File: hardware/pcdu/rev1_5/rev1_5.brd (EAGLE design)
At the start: 90 x 16.2 mm, 11 parts, among them IC1 74HC595N, X1 MUSBV, X2 MUSBV, X3 MUSBV, X4 MUSBV, X7 22-23-2041, X8 22-23-2041

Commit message: Added PCU board, updated revision 5 PDU board
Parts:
- removed X6: (no value), con-wago-500:W237-102
- moved X5 0.91 mm to (24.1, 12.3)
- moved U$1 0.91 mm to (22.6, 5.94)
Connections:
- net GND: no longer X6.2
- net VCC: no longer X6.1
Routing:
- net GND: track 8.89 -> 0.00 mm
- net N$2: track 39.3 -> 45.1 mm
- net SIN: track 50.2 -> 47.8 mm
- net N$1: track 44.9 -> 46.0 mm
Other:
- board text added: "5VPDU Rev1.5"
- board text added: "GND"
- board text added: "IN"
- board text added: "OUT"
- board text added: "RCK"
- board text added: "SCK"
- board text added: "SER"
- board text added: "VCC"
- board text added: "by Denis Lavrov"
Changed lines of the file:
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@@
 <setting verticaltext="up"/>
 </settings>
-<grid distance="12" unitdist="mil" unit="mil" style="lines" multiple="1" display="no" altdistance="0.025" altunitdist="inch" altunit="inch"/>
+<grid distance="12" unitdist="mil" unit="mil" style="lines" multiple="1" display="no" altdistance="6" altunitdist="mil" altunit="mil"/>
 <layers>
 <layer number="1" name="Top" color="4" fill="1" visible="yes" active="yes"/>
@@
 <wire x1="90" y1="16.18" x2="0" y2="16.18" width="0" layer="20"/>
 <wire x1="0" y1="16.18" x2="0" y2="0" width="0" layer="20"/>
+<text x="73.152" y="13.4112" size="1.778" layer="21">5VPDU Rev1.5</text>
+<text x="71.628" y="0.6096" size="1.778" layer="21">by Denis Lavrov</text>
+<text x="11.2776" y="0.9144" size="1.778" layer="21">IN</text>
+<text x="11.2776" y="14.0208" size="1.778" layer="21">OUT</text>
+<text x="2.7432" y="8.5344" size="0.6096" layer="21" rot="R180">GND</text>
+<text x="5.1816" y="8.5344" size="0.6096" layer="21" rot="R180">RCK</text>
+<text x="7.62" y="8.5344" size="0.6096" layer="21" rot="R180">SCK</text>
+<text x="10.0584" y="8.5344" size="0.6096" layer="21" rot="R180">SER</text>
+<text x="20.1168" y="5.4864" size="1.016" layer="21">VCC</text>
+<text x="25.273" y="5.4864" size="1.016" layer="21">GND</text>
 </plain>
 <attributes>
@@
 <elements>
 <element name="IC1" library="74xx-eu" package="DIL16" value="74HC595N" x="49.53" y="7.47" rot="R180"/>
-<element name="U$1" library="FDC6305N" package="FDC6305" value="FDC6305N" x="22.5552" y="6.858" rot="MR90"/>
+<element name="U$1" library="FDC6305N" package="FDC6305" value="FDC6305N" x="22.5552" y="5.9436" rot="MR90"/>
 <element name="U$2" library="FDC6305N" package="FDC6305" value="FDC6305N" x="73.7616" y="9.652" rot="MR90"/>
-<element name="X5" library="con-wago-500" package="W237-102" value="" x="24.13" y="13.2588">
-<attribute name="OC_NEWARK" value="70K9898" x="24.13" y="13.2588" size="1.778" layer="27" display="off"/>
-<attribute name="MF" value="" x="24.13" y="13.2588" size="1.778" layer="27" display="off"/>
-<attribute name="OC_FARNELL" value="unknown" x="24.13" y="13.2588" size="1.778" layer="27" display="off"/>
-<attribute name="MPN" value="237-102" x="24.13" y="13.2588" size="1.778" layer="27" display="off"/>
+<element name="X5" library="con-wago-500" package="W237-102" value="" x="24.13" y="12.3444">
+<attribute name="OC_NEWARK" value="70K9898" x="24.13" y="12.3444" size="1.778" layer="27" display="off"/>
+<attribute name="MF" value="" x="24.13" y="12.3444" size="1.778" layer="27" display="off"/>
+<attribute name="OC_FARNELL" value="unknown" x="24.13" y="12.3444" size="1.778" layer="27" display="off"/>
+<attribute name="MPN" value="237-102" x="24.13" y="12.3444" size="1.778" layer="27" display="off"/>
 </element>
-<element name="X6" library="con-wago-500" package="W237-102" value="" x="24.13" y="1.8796" rot="R180">
-<attribute name="OC_NEWARK" value="70K9898" x="24.13" y="1.8796" size="1.778" layer="27" rot="R180" display="off"/>
-<attribute name="MF" value="" x="24.13" y="1.8796" size="1.778" layer="27" rot="R180" display="off"/>
-<attribute name="OC_FARNELL" value="unknown" x="24.13" y="1.8796" size="1.778" layer="27" rot="R180" display="off"/>
-<attribute name="MPN" value="237-102" x="24.13" y="1.8796" size="1.778" layer="27" rot="R180" display="off"/>
-</element>
-<element name="X7" library="con-molex" package="22-23-2041" value="22-23-2041" x="5.73" y="3.81" rot="R180">
+<element name="X7" library="con-molex" package="22-23-2041" value="22-23-2041" x="5.73" y="3.81" smashed="yes" rot="R180">
 <attribute name="OC_NEWARK" value="38C0355" x="5.73" y="3.81" size="1.778" layer="27" rot="R180" display="off"/>
 <attribute name="MF" value="MOLEX" x="5.73" y="3.81" size="1.778" layer="27" rot="R180" display="off"/>
@@
 <attribute name="MPN" value="22-23-2041" x="5.73" y="3.81" size="1.778" layer="27" rot="R180" display="off"/>
 </element>
-<element name="X8" library="con-molex" package="22-23-2041" value="22-23-2041" x="5.73" y="12.7" rot="R180">
+<element name="X8" library="con-molex" package="22-23-2041" value="22-23-2041" x="5.73" y="12.7" smashed="yes" rot="R180">
 <attribute name="OC_NEWARK" value="38C0355" x="5.73" y="12.7" size="1.778" layer="27" rot="R180" display="off"/>
 <attribute name="MF" value="MOLEX" x="5.73" y="12.7" size="1.778" layer="27" rot="R180" display="off"/>
@@
 <signal name="VCC">
 <contactref element="X5" pad="1"/>
-<contactref element="X6" pad="1"/>
 <contactref element="IC1" pad="16"/>
 <contactref element="IC1" pad="10"/>
@@
 <contactref element="U$2" pad="S2"/>
 <contactref element="X5" pad="2"/>
-<contactref element="X6" pad="2"/>
 <contactref element="X7" pad="4"/>
 <contactref element="X8" pad="4"/>
@@
 <contactref element="U$1" pad="S1"/>
 <contactref element="U$2" pad="S1"/>
-<wire x1="1.92" y1="12.7" x2="1.92" y2="3.81" width="0.1524" layer="1"/>
 <polygon width="0.1524" layer="16">
 <vertex x="0" y="16.1544"/>
@@
 <contactref element="IC1" pad="15"/>
 <contactref element="U$1" pad="G1"/>
-<wire x1="55.88" y1="3.66" x2="55.88" y2="5.7912" width="0.1524" layer="16"/>
-<wire x1="55.88" y1="5.7912" x2="37.1856" y2="5.7912" width="0.1524" layer="16"/>
-<wire x1="37.1856" y1="5.7912" x2="37.1856" y2="11.2776" width="0.1524" layer="16"/>
-<wire x1="37.1856" y1="11.2776" x2="32.9184" y2="11.2776" width="0.1524" layer="16"/>
-<wire x1="32.9184" y1="11.2776" x2="32.9184" y2="7.9248" width="0.1524" layer="16"/>
-<wire x1="32.9184" y1="7.9248" x2="23.1648" y2="7.9248" width="0.1524" layer="16"/>
-<wire x1="23.1648" y1="7.9248" x2="23.1648" y2="9.058" width="0.1524" layer="16"/>
-<wire x1="23.1648" y1="9.058" x2="23.1052" y2="9.058" width="0.1524" layer="16"/>
+<wire x1="55.88" y1="3.66" x2="55.88" y2="7.0104" width="0.1524" layer="16"/>
+<wire x1="55.88" y1="7.0104" x2="37.4904" y2="7.0104" width="0.1524" layer="16"/>
+<wire x1="37.4904" y1="7.0104" x2="37.4904" y2="11.2776" width="0.1524" layer="16"/>
+<wire x1="37.4904" y1="11.2776" x2="32.3088" y2="11.2776" width="0.1524" layer="16"/>
+<wire x1="32.3088" y1="11.2776" x2="32.3088" y2="6.858" width="0.1524" layer="16"/>
+<wire x1="32.3088" y1="6.858" x2="23.1648" y2="6.858" width="0.1524" layer="16"/>
+<wire x1="23.1648" y1="6.858" x2="23.1648" y2="7.8388" width="0.1524" layer="16"/>
+<wire x1="23.1648" y1="7.8388" x2="23.1052" y2="8.1436" width="0.1524" layer="16"/>
 </signal>
 <signal name="N$2">
 <contactref element="IC1" pad="1"/>
 <contactref element="U$1" pad="G2"/>
-<wire x1="58.42" y1="11.28" x2="58.42" y2="9.7536" width="0.1524" layer="16"/>
-<wire x1="58.42" y1="9.7536" x2="38.1" y2="9.7536" width="0.1524" layer="16"/>
-<wire x1="38.1" y1="9.7536" x2="38.1" y2="11.5824" width="0.1524" layer="16"/>
-<wire x1="38.1" y1="11.5824" x2="32.6136" y2="11.5824" width="0.1524" layer="16"/>
-<wire x1="32.6136" y1="11.5824" x2="32.6136" y2="9.058" width="0.1524" layer="16"/>
-<wire x1="32.6136" y1="9.058" x2="25.0052" y2="9.058" width="0.1524" layer="16"/>
+<wire x1="58.42" y1="11.28" x2="58.42" y2="7.62" width="0.1524" layer="16"/>
+<wire x1="58.42" y1="7.62" x2="38.1" y2="7.62" width="0.1524" layer="16"/>
+<wire x1="38.1" y1="7.62" x2="38.1" y2="11.8872" width="0.1524" layer="16"/>
+<wire x1="38.1" y1="11.8872" x2="31.6992" y2="11.8872" width="0.1524" layer="16"/>
+<wire x1="31.6992" y1="11.8872" x2="31.6992" y2="8.1436" width="0.1524" layer="16"/>
+<wire x1="31.6992" y1="8.1436" x2="25.0052" y2="8.1436" width="0.1524" layer="16"/>
 </signal>
 <signal name="N$3">
@@
 <contactref element="IC1" pad="14"/>
 <wire x1="9.54" y1="3.81" x2="9.4488" y2="3.81" width="0.1524" layer="16"/>
-<wire x1="9.4488" y1="3.81" x2="9.4488" y2="0.6096" width="0.1524" layer="16"/>
-<wire x1="9.4488" y1="0.6096" x2="53.34" y2="0.6096" width="0.1524" layer="16"/>
-<wire x1="53.34" y1="0.6096" x2="53.34" y2="3.66" width="0.1524" layer="16"/>
+<wire x1="9.4488" y1="3.81" x2="9.4488" y2="1.8288" width="0.1524" layer="16"/>
+<wire x1="9.4488" y1="1.8288" x2="53.34" y2="1.8288" width="0.1524" layer="16"/>
+<wire x1="53.34" y1="1.8288" x2="53.34" y2="3.66" width="0.1524" layer="16"/>
 </signal>
 <signal name="SCK">
@@
 <wire x1="15.325" y1="5.7" x2="16.05" y2="5.7" width="0.762" layer="16"/>
 <wire x1="16.05" y1="5.7" x2="16.25" y2="5.5" width="0.762" layer="16"/>
-<wire x1="23.1052" y1="6.458" x2="22.1472" y2="5.5" width="0.762" layer="16"/>
+<wire x1="23.1052" y1="5.5436" x2="22.1472" y2="5.5" width="0.762" layer="16"/>
 <wire x1="22.1472" y1="5.5" x2="16.25" y2="5.5" width="0.762" layer="16"/>
 </signal>
@@
 <wire x1="35.325" y1="5.7" x2="36.05" y2="5.7" width="0.762" layer="16"/>
 <wire x1="36.05" y1="5.7" x2="36.25" y2="5.5" width="0.762" layer="16"/>
-<wire x1="33.75" y1="5.5" x2="33.75" y2="4.635" width="0.762" layer="16"/>
+<wire x1="33.75" y1="5.4864" x2="33.75" y2="4.635" width="0.762" layer="16"/>
 <wire x1="33.75" y1="4.635" x2="34.71" y2="3.675" width="0.762" layer="16"/>
-<wire x1="33.75" y1="5.5" x2="33.75" y2="6.096" width="0.762" layer="16"/>
-<wire x1="33.75" y1="6.096" x2="33.75" y2="8.5" width="0.762" layer="16"/>
+<wire x1="33.75" y1="5.4864" x2="33.75" y2="8.5" width="0.762" layer="16"/>
 <wire x1="33.75" y1="8.5" x2="33.75" y2="9.365" width="0.762" layer="16"/>
 <wire x1="33.75" y1="9.365" x2="34.71" y2="10.325" width="0.762" layer="16"/>
-<wire x1="25.0052" y1="6.458" x2="25.3672" y2="6.096" width="0.762" layer="16"/>
-<wire x1="25.3672" y1="6.096" x2="33.75" y2="6.096" width="0.762" layer="16"/>
+<wire x1="25.0052" y1="5.5436" x2="25.3672" y2="5.4864" width="0.762" layer="16"/>
+<wire x1="25.3672" y1="5.4864" x2="33.75" y2="5.4864" width="0.762" layer="16"/>
+<wire x1="33.75" y1="5.4864" x2="33.75" y2="5.5" width="0" layer="19" extent="16-16"/>
 </signal>
 <signal name="N$11">

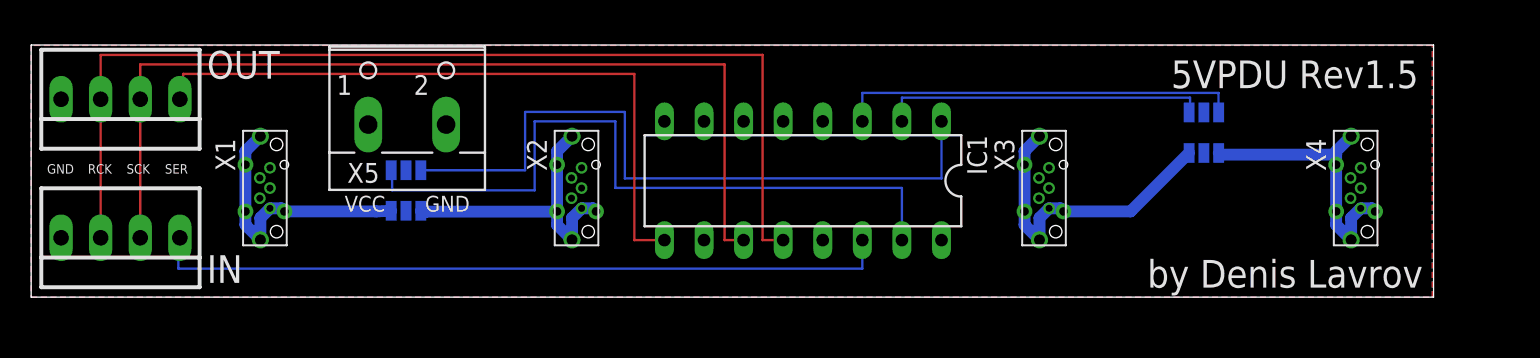
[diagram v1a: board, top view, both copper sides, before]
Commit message: Added software controlled LED indicators to rev1_5
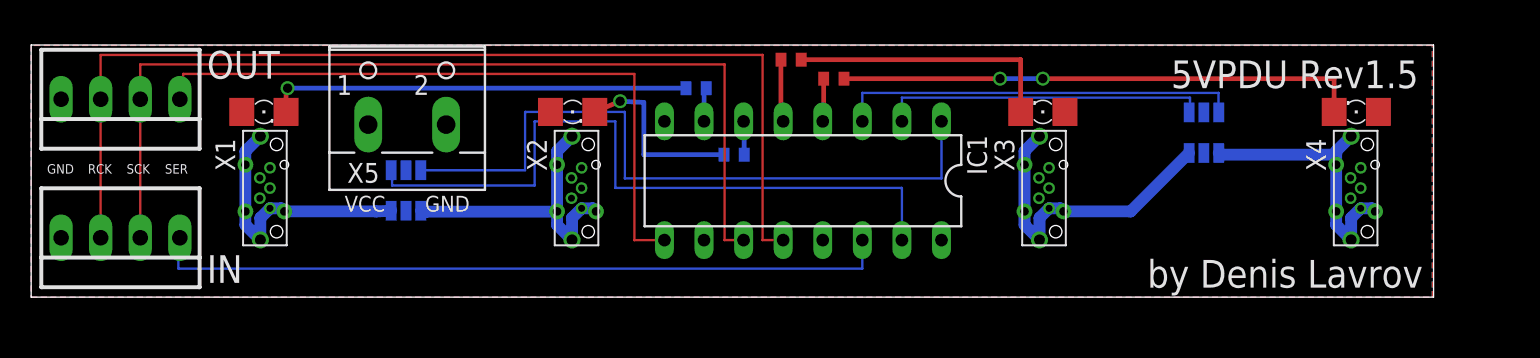
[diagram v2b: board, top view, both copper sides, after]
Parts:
- added LED1, LED2, LED3, LED4: (no value), eagle-ltspice:LED_1206
- added R1, R2, R3, R4: (no value), eagle-ltspice:R1005
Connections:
- new net N$13: IC1.4, R1.1
- new net N$14: IC1.5, R2.1
- new net N$15: IC1.6, R3.1
- new net N$16: IC1.7, R4.1
- new net N$5: LED4.C, R1.2
- new net N$6: LED3.C, R2.2
- new net N$7: LED2.C, R3.2
- new net N$8: LED1.C, R4.2
- net VCC: now also LED1.A, LED2.A, LED3.A, LED4.A
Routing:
- net N$5: track 0.00 -> 33.6 mm, vias 0 -> 2
- net N$8: track 0.00 -> 27.2 mm, vias 0 -> 1
- net N$6: track 0.00 -> 17.4 mm
- net N$7: track 0.00 -> 11.8 mm, vias 0 -> 1
- net N$14: track 0.00 -> 4.10 mm
- net N$13: track 0.00 -> 2.74 mm
- net N$16: track 0.00 -> 2.27 mm
- net N$15: track 0.00 -> 2.18 mm
- net N$1: track 46.0 -> 45.4 mm
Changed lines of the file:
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@@
 <?xml version="1.0" encoding="utf-8"?>
 <!DOCTYPE eagle SYSTEM "eagle.dtd">
-<eagle version="7.6.0">
+<eagle version="7.7.0">
 <drawing>
 <settings>
@@
 <layer number="97" name="Info" color="7" fill="1" visible="no" active="no"/>
 <layer number="98" name="Guide" color="6" fill="1" visible="no" active="no"/>
+<layer number="99" name="SpiceOrder" color="5" fill="1" visible="no" active="no"/>
 </layers>
 <board>
@@
 <element name="X3" library="MUSBV" package="MUSBV" value="MUSBV" x="65" y="7" rot="R270"/>
 <element name="X4" library="MUSBV" package="MUSBV" value="MUSBV" x="85" y="7" rot="R270"/>
+<element name="LED1" library="eagle-ltspice" package="LED_1206" value="" x="14.9352" y="11.8872" smashed="yes">
+<attribute name="SPICEPREFIX" value="D" x="14.9352" y="11.8872" size="1.778" layer="27" display="off"/>
+<attribute name="SPICEMODEL" value="NONE" x="14.9352" y="11.8872" size="1.778" layer="27" display="off"/>
+<attribute name="SPICETYPE" value="diode" x="14.9352" y="11.8872" size="1.778" layer="27" display="off"/>
+<attribute name="VALUE" x="13.6652" y="9.3472" size="1.27" layer="27"/>
+</element>
+<element name="LED2" library="eagle-ltspice" package="LED_1206" value="" x="34.7472" y="11.8872" smashed="yes">
+<attribute name="SPICEPREFIX" value="D" x="34.7472" y="11.8872" size="1.778" layer="27" display="off"/>
+<attribute name="SPICEMODEL" value="NONE" x="34.7472" y="11.8872" size="1.778" layer="27" display="off"/>
+<attribute name="SPICETYPE" value="diode" x="34.7472" y="11.8872" size="1.778" layer="27" display="off"/>
+<attribute name="VALUE" x="33.4772" y="9.3472" size="1.27" layer="27"/>
+</element>
+<element name="LED3" library="eagle-ltspice" package="LED_1206" value="" x="64.9224" y="11.8872" smashed="yes" rot="R180">
+<attribute name="SPICEPREFIX" value="D" x="64.9224" y="11.8872" size="1.778" layer="27" rot="R180" display="off"/>
+<attribute name="SPICEMODEL" value="NONE" x="64.9224" y="11.8872" size="1.778" layer="27" rot="R180" display="off"/>
+<attribute name="SPICETYPE" value="diode" x="64.9224" y="11.8872" size="1.778" layer="27" rot="R180" display="off"/>
+<attribute name="VALUE" x="66.1924" y="14.4272" size="1.27" layer="27" rot="R180"/>
+</element>
+<element name="LED4" library="eagle-ltspice" package="LED_1206" value="" x="85.0392" y="11.8872" smashed="yes" rot="R180">
+<attribute name="SPICEPREFIX" value="D" x="85.0392" y="11.8872" size="1.778" layer="27" rot="R180" display="off"/>
+<attribute name="SPICEMODEL" value="NONE" x="85.0392" y="11.8872" size="1.778" layer="27" rot="R180" display="off"/>
+<attribute name="SPICETYPE" value="diode" x="85.0392" y="11.8872" size="1.778" layer="27" rot="R180" display="off"/>
+<attribute name="VALUE" x="86.3092" y="14.4272" size="1.27" layer="27" rot="R180"/>
+</element>
+<element name="R1" library="eagle-ltspice" package="R1005" value="" x="51.5112" y="14.0208" smashed="yes">
+<attribute name="SPICEPREFIX" value="R" x="51.5112" y="14.0208" size="1.778" layer="27" display="off"/>
+<attribute name="SPICEMODEL" value="NONE" x="51.5112" y="14.0208" size="1.778" layer="27" display="off"/>
+<attribute name="VALUE" x="50.8762" y="12.1158" size="1.27" layer="27"/>
+</element>
+<element name="R2" library="eagle-ltspice" package="R1005" value="" x="48.768" y="15.24" smashed="yes">
+<attribute name="SPICEPREFIX" value="R" x="48.768" y="15.24" size="1.778" layer="27" display="off"/>
+<attribute name="SPICEMODEL" value="NONE" x="48.768" y="15.24" size="1.778" layer="27" display="off"/>
+<attribute name="VALUE" x="48.133" y="13.335" size="1.27" layer="27"/>
+</element>
+<element name="R3" library="eagle-ltspice" package="R1005" value="" x="45.1104" y="9.144" smashed="yes" rot="MR0">
+<attribute name="SPICEPREFIX" value="R" x="45.1104" y="9.144" size="1.778" layer="28" rot="MR0" display="off"/>
+<attribute name="SPICEMODEL" value="NONE" x="45.1104" y="9.144" size="1.778" layer="28" rot="MR0" display="off"/>
+<attribute name="VALUE" x="45.7454" y="7.239" size="1.27" layer="28" rot="MR0"/>
+</element>
+<element name="R4" library="eagle-ltspice" package="R1005" value="" x="42.672" y="13.4112" smashed="yes" rot="MR0">
+<attribute name="SPICEPREFIX" value="R" x="42.672" y="13.4112" size="1.778" layer="28" rot="MR0" display="off"/>
+<attribute name="SPICEMODEL" value="NONE" x="42.672" y="13.4112" size="1.778" layer="28" rot="MR0" display="off"/>
+<attribute name="VALUE" x="43.307" y="11.5062" size="1.27" layer="28" rot="MR0"/>
+</element>
 </elements>
 <signals>
@@
 <contactref element="X3" pad="1"/>
 <contactref element="X4" pad="1"/>
-<polygon width="0.1524" layer="1">
+<contactref element="LED4" pad="A"/>
+<contactref element="LED3" pad="A"/>
+<contactref element="LED2" pad="A"/>
+<contactref element="LED1" pad="A"/>
+<polygon width="0.3048" layer="1">
 <vertex x="0" y="16.1544"/>
 <vertex x="0" y="0"/>
@@
 <contactref element="U$1" pad="S1"/>
 <contactref element="U$2" pad="S1"/>
-<polygon width="0.1524" layer="16">
+<polygon width="0.3048" layer="16">
 <vertex x="0" y="16.1544"/>
 <vertex x="0" y="0"/>
@@
 <wire x1="37.4904" y1="7.0104" x2="37.4904" y2="11.2776" width="0.1524" layer="16"/>
 <wire x1="37.4904" y1="11.2776" x2="32.3088" y2="11.2776" width="0.1524" layer="16"/>
-<wire x1="32.3088" y1="11.2776" x2="32.3088" y2="6.858" width="0.1524" layer="16"/>
-<wire x1="32.3088" y1="6.858" x2="23.1648" y2="6.858" width="0.1524" layer="16"/>
-<wire x1="23.1648" y1="6.858" x2="23.1648" y2="7.8388" width="0.1524" layer="16"/>
+<wire x1="32.3088" y1="11.2776" x2="32.3088" y2="7.1628" width="0.1524" layer="16"/>
+<wire x1="32.3088" y1="7.1628" x2="23.1648" y2="7.1628" width="0.1524" layer="16"/>
+<wire x1="23.1648" y1="7.1628" x2="23.1648" y2="7.8388" width="0.1524" layer="16"/>
 <wire x1="23.1648" y1="7.8388" x2="23.1052" y2="8.1436" width="0.1524" layer="16"/>
 </signal>
@@
 <wire x1="76.3196" y1="9.144" x2="83.75" y2="9.144" width="0.762" layer="16"/>
 </signal>
+<signal name="N$13">
+<contactref element="IC1" pad="4"/>
+<contactref element="R1" pad="1"/>
+<wire x1="50.8612" y1="11.28" x2="50.8612" y2="14.0208" width="0.3048" layer="1"/>
+<wire x1="50.8612" y1="11.28" x2="50.8" y2="11.28" width="0" layer="19" extent="1-1"/>
+</signal>
+<signal name="N$14">
+<contactref element="IC1" pad="5"/>
+<contactref element="R2" pad="1"/>
+<wire x1="48.26" y1="11.28" x2="48.118" y2="11.28" width="0.3048" layer="1"/>
+<wire x1="48.118" y1="11.28" x2="48.118" y2="15.24" width="0.3048" layer="1"/>
+</signal>
+<signal name="N$15">
+<contactref element="IC1" pad="6"/>
+<contactref element="R3" pad="1"/>
+<wire x1="45.72" y1="11.28" x2="45.7604" y2="11.28" width="0.3048" layer="16"/>
+<wire x1="45.7604" y1="11.28" x2="45.7604" y2="9.144" width="0.3048" layer="16"/>
+</signal>
+<signal name="N$16">
+<contactref element="IC1" pad="7"/>
+<contactref element="R4" pad="1"/>
+<wire x1="43.322" y1="13.4112" x2="43.18" y2="13.4112" width="0.3048" layer="16"/>
+<wire x1="43.18" y1="13.4112" x2="43.18" y2="11.28" width="0.3048" layer="16"/>
+</signal>
+<signal name="N$5">
+<contactref element="LED4" pad="C"/>
+<contactref element="R1" pad="2"/>
+<wire x1="52.1612" y1="14.0208" x2="62.1792" y2="14.0208" width="0.3048" layer="1"/>
+<via x="62.1792" y="14.0208" extent="1-16" drill="0.6"/>
+<wire x1="62.1792" y1="14.0208" x2="64.9224" y2="14.0208" width="0.3048" layer="16"/>
+<via x="64.9224" y="14.0208" extent="1-16" drill="0.6"/>
+<wire x1="64.9224" y1="14.0208" x2="83.6172" y2="14.0208" width="0.3048" layer="1"/>
+<wire x1="83.6172" y1="14.0208" x2="83.6172" y2="11.8872" width="0.3048" layer="1"/>
+</signal>
+<signal name="N$6">
+<contactref element="LED3" pad="C"/>
+<contactref element="R2" pad="2"/>
+<wire x1="49.418" y1="15.24" x2="63.5004" y2="15.24" width="0.3048" layer="1"/>
+<wire x1="63.5004" y1="15.24" x2="63.5004" y2="11.8872" width="0.3048" layer="1"/>
+</signal>
+<signal name="N$7">
+<contactref element="LED2" pad="C"/>
+<contactref element="R3" pad="2"/>
+<wire x1="44.4604" y1="9.144" x2="39.3192" y2="9.144" width="0.3048" layer="16"/>
+<wire x1="39.3192" y1="9.144" x2="39.3192" y2="12.4968" width="0.3048" layer="16"/>
+<wire x1="39.3192" y1="12.4968" x2="37.7952" y2="12.573" width="0.3048" layer="16"/>
+<via x="37.7952" y="12.573" extent="1-16" drill="0.6"/>
+<wire x1="37.7952" y1="12.573" x2="36.1692" y2="11.8872" width="0.3048" layer="1"/>
+</signal>
+<signal name="N$8">
+<contactref element="LED1" pad="C"/>
+<contactref element="R4" pad="2"/>
+<wire x1="42.022" y1="13.4112" x2="16.4592" y2="13.4112" width="0.3048" layer="16"/>
+<via x="16.4592" y="13.4112" extent="1-16" drill="0.6"/>
+<wire x1="16.4592" y1="13.4112" x2="16.3572" y2="13.4112" width="0.3048" layer="1"/>
+<wire x1="16.3572" y1="13.4112" x2="16.3572" y2="11.8872" width="0.3048" layer="1"/>
+</signal>
 </signals>
